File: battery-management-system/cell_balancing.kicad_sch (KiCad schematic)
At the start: 28 parts, among them Q14 DMN3404L, Q15 DMN3404L, Q16 DMN3404L, Q17 DMN3404L, Q18 DMN3404L, Q19 DMN3404L, Q20 DMN3404L, Q21 DMN3404L, Q22 DMN3404L, Q23 DMN3404L, Q24 DMN3404L, Q25 DMN3404L, Q26 DMN3404L, Q27 DMN3404L, Q28 DMN3404L, Q29 DMN3404L, Q30 DMN3404L, Q31 DMN3404L, U16 MC74VHC139

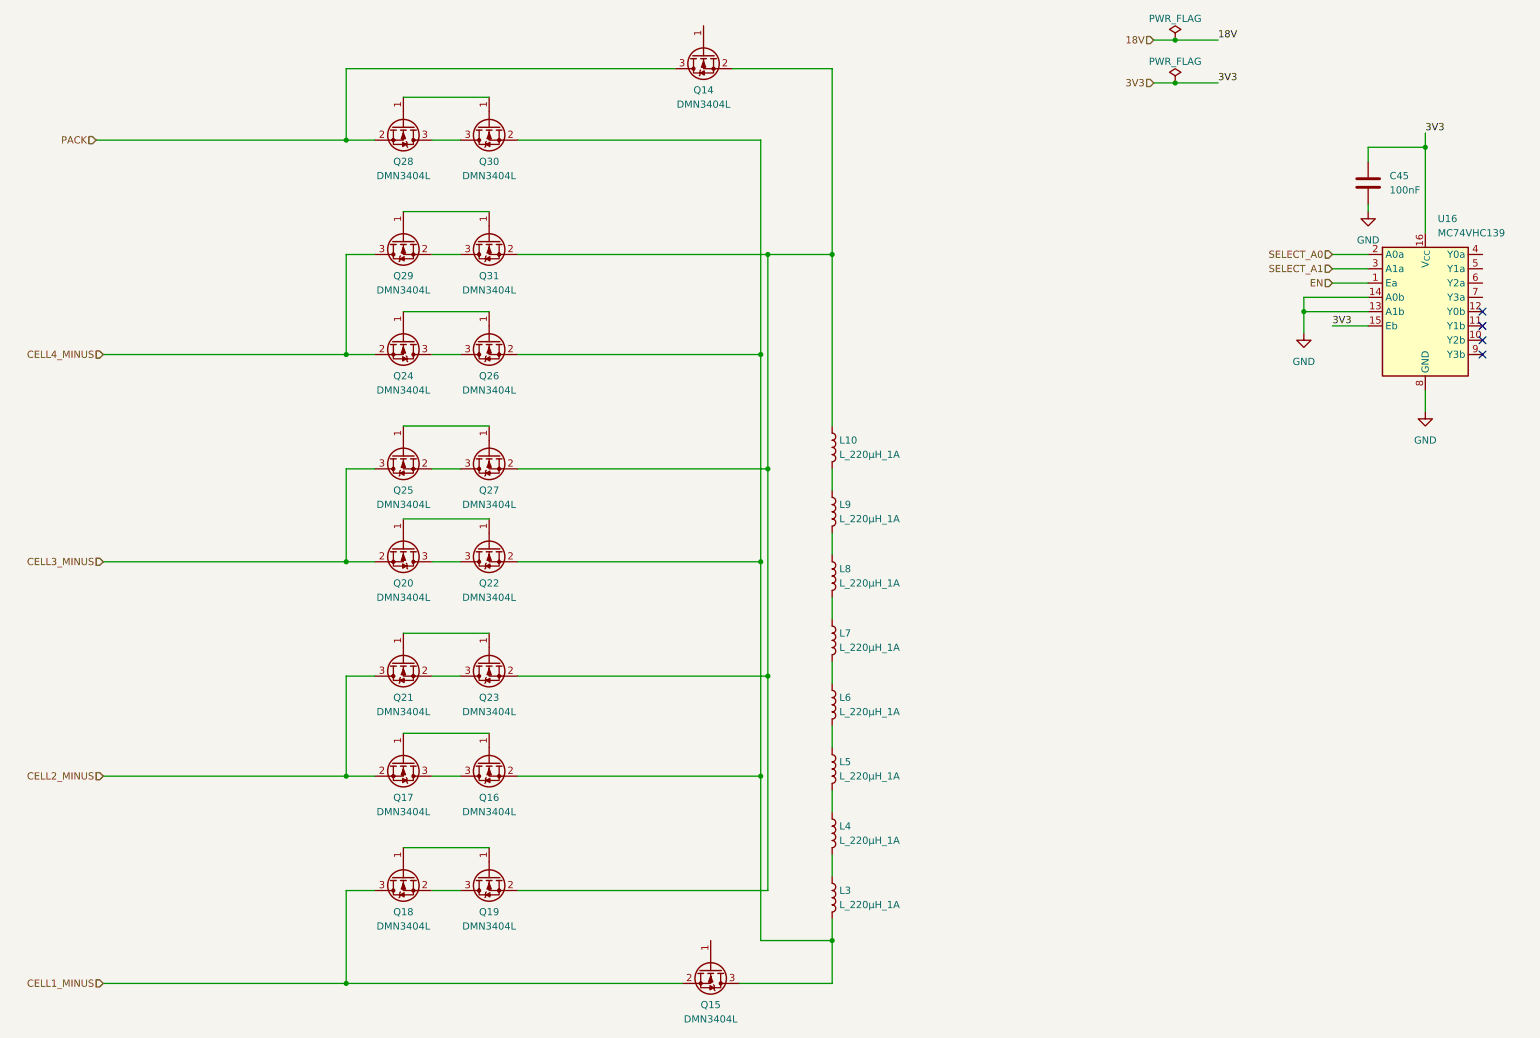
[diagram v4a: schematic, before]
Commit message: finish cell balancing changes
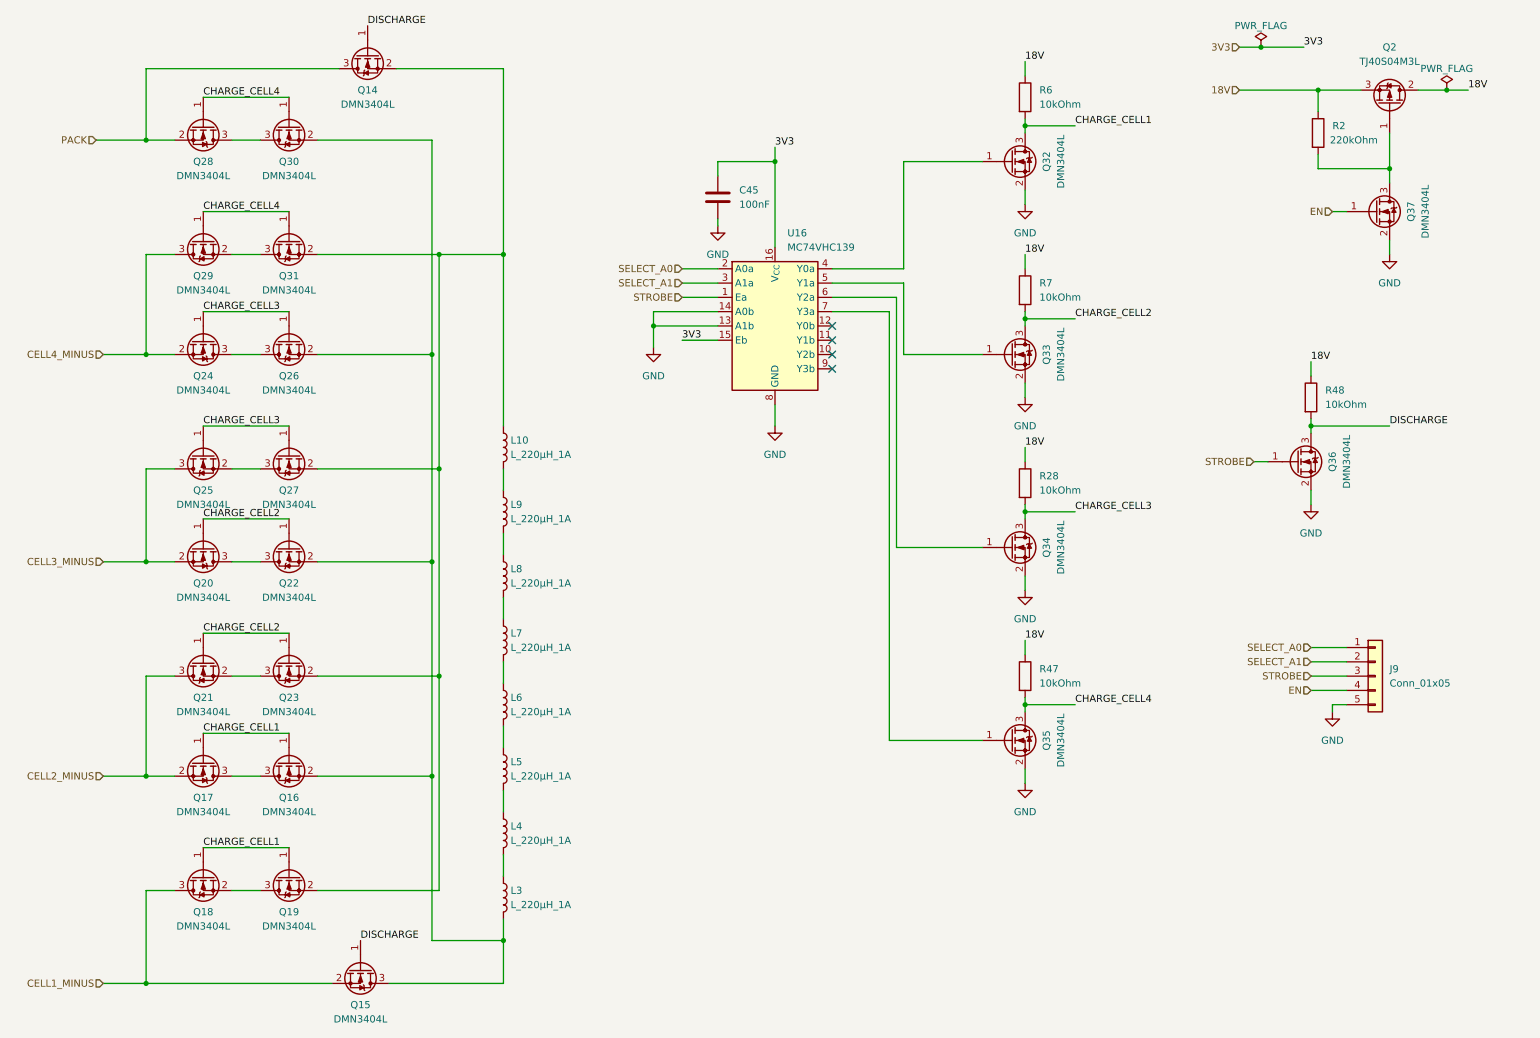
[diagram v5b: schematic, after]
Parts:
- added J9: Conn_01x05, benediktibk:PinHeader_1x05_P2.54mm_Vertical, symbol benediktibk:Conn_01x05
- added Q2: TJ40S04M3L, benediktibk:TO-252-2, symbol benediktibk:TJ40S04M3L
- added Q32, Q33, Q34, Q35, Q36, Q37: DMN3404L, benediktibk:SOT-23, symbol benediktibk:DMN3404L
- added R2: 220kOhm, benediktibk:R_0603_1608Metric_Pad0.98x0.95mm_HandSolder, symbol benediktibk:R_220kOhm_SMD_0603_100mW_1%
- added R28, R47, R48, R6, R7: 10kOhm, benediktibk:R_0603_1608Metric_Pad0.98x0.95mm_HandSolder, symbol benediktibk:R_10kOhm_SMD_0603_100mW_1%
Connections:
- net 18V: now also Q2.2 (D), Q2.3 (S), R2.1, R28.1, R47.1, R48.1, R6.1, R7.1
- net EN: now also J9.4 (Pin_4), Q37.1 (G); no longer U16.1 (Ea)
- net GND: now also J9.5 (Pin_5), Q32.2 (S), Q33.2 (S), Q34.2 (S), Q35.2 (S), Q36.2 (S), Q37.2 (S)
- net SELECT_A0: now also J9.1 (Pin_1)
- net SELECT_A1: now also J9.2 (Pin_2)
- net CHARGE_CELL4: now reaches Q29.1 (G), Q31.1 (G)
- net CHARGE_CELL4: now also Q28.1 (G), Q30.1 (G), Q35.3 (D), R47.2
- net DISCHARGE: now reaches Q14.1 (G)
- net DISCHARGE: now also Q15.1 (G), Q36.3 (D), R48.2
- net CHARGE_CELL2: now reaches Q21.1 (G), Q23.1 (G)
- net CHARGE_CELL2: now also Q20.1 (G), Q22.1 (G), Q33.3 (D), R7.2
- net CHARGE_CELL3: now reaches Q24.1 (G), Q26.1 (G)
- net CHARGE_CELL3: now also Q25.1 (G), Q27.1 (G), Q34.3 (D), R28.2
- net at U16.4 (Y0a): now also Q32.1 (G)
- net at U16.5 (Y1a): now also Q33.1 (G)
- net at U16.6 (Y2a): now also Q34.1 (G)
- net at U16.7 (Y3a): now also Q35.1 (G)
- net CHARGE_CELL1: now reaches Q18.1 (G), Q19.1 (G)
- net CHARGE_CELL1: now also Q16.1 (G), Q17.1 (G), Q32.3 (D), R6.2
- new net: Q2.1 (G), Q37.3 (D), R2.2
- new net STROBE: J9.3 (Pin_3), Q36.1 (G), U16.1 (Ea)
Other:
- moved on the sheet: C45, L10, L3, L4, L5, L6, L7, L8, L9, Q14, Q15, Q16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

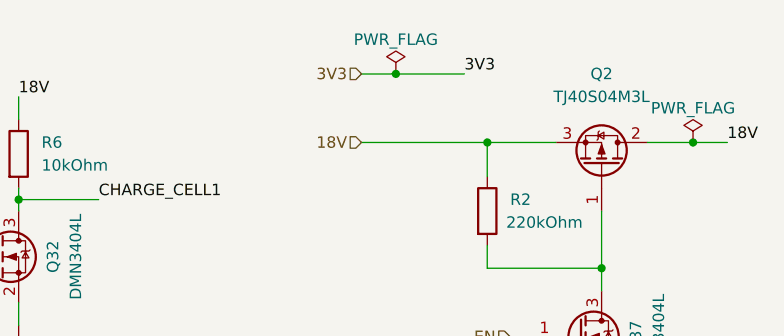
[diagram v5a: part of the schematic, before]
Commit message: fix electrical rule check errors
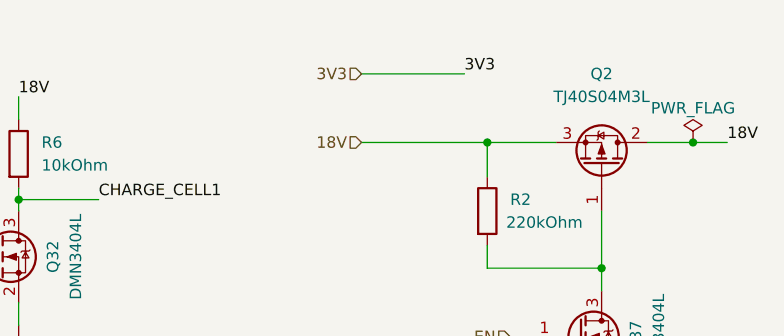
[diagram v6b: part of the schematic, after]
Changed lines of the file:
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@@
   (junction (at 247.65 26.67) (diameter 0) (color 0 0 0 0)
-  )
-  (junction (at 237.49 19.05) (diameter 0) (color 0 0 0 0)
   )
   (junction (at 260.35 40.64) (diameter 0) (color 0 0 0 0)
@@
     (stroke (width 0) (type default))
   )
-  (wire (pts (xy 237.49 19.05) (xy 245.11 19.05))
-    (stroke (width 0) (type default))
-  )
   (wire (pts (xy 195.58 135.89) (xy 204.47 135.89))
     (stroke (width 0) (type default))
@@
     (stroke (width 0) (type default))
   )
-  (wire (pts (xy 233.68 19.05) (xy 237.49 19.05))
+  (wire (pts (xy 233.68 19.05) (xy 245.11 19.05))
     (stroke (width 0) (type default))
   )
@@
         )
       )
-    )
-  )
-  (symbol (lib_id "power:PWR_FLAG") (at 237.49 19.05 0) (unit 1)
-    (in_bom yes) (on_board yes) (dnp no)
-    (property "Reference" "#FLG01" (at 237.49 17.145 0)
-      (effects (font (size 1.27 1.27)) hide)
-    )
-    (property "Value" "PWR_FLAG" (at 237.49 15.24 0)
-      (effects (font (size 1.27 1.27)))
-    )
-    (property "Footprint" "" (at 237.49 19.05 0)
-      (effects (font (size 1.27 1.27)) hide)
-    )
-    (property "Datasheet" "~" (at 237.49 19.05 0)
-      (effects (font (size 1.27 1.27)) hide)
-    )
-    (pin "1")
-    (instances
-      (project "battery-management-system"
-        (path "/5272f0ff-3069-41a9-bca2-80beede8b4b2/b1377397-46a1-4623-af59-88e4e694ca35"
-          (reference "#FLG01") (unit 1)
-        )
-        (path "/5272f0ff-3069-41a9-bca2-80beede8b4b2/3d1b4e38-a765-486c-a970-a0d54d5b41d9"
-          (reference "#FLG010") (unit 1)
-        )
-      )

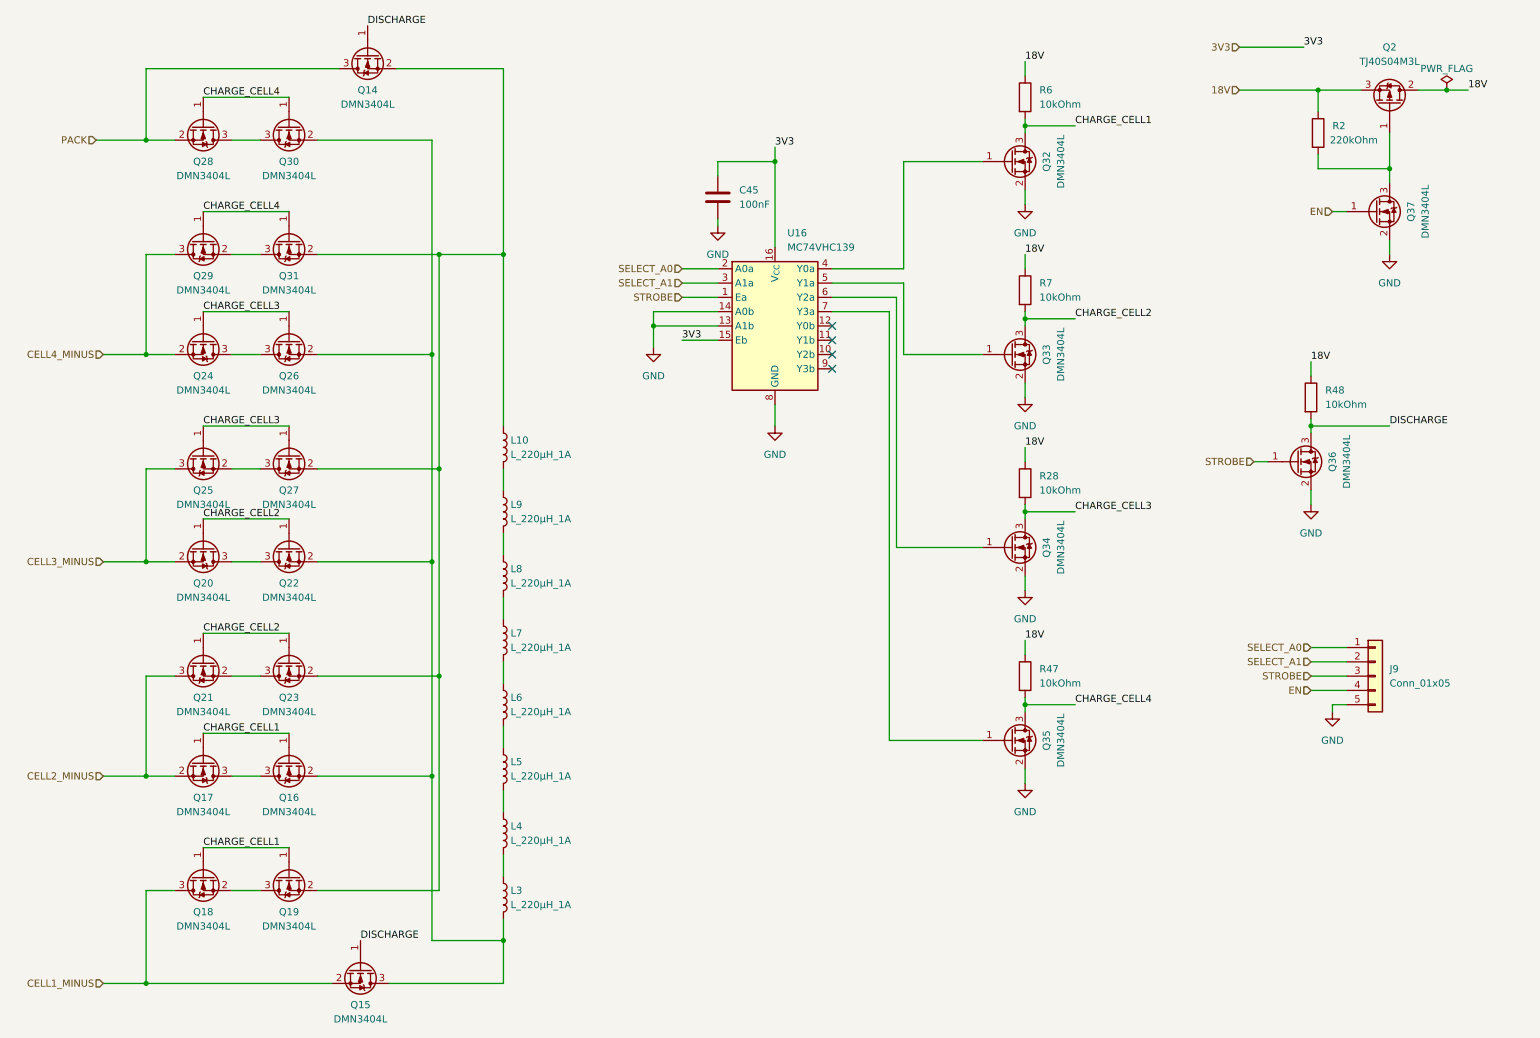
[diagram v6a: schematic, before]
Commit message: add enable input for cell measurement
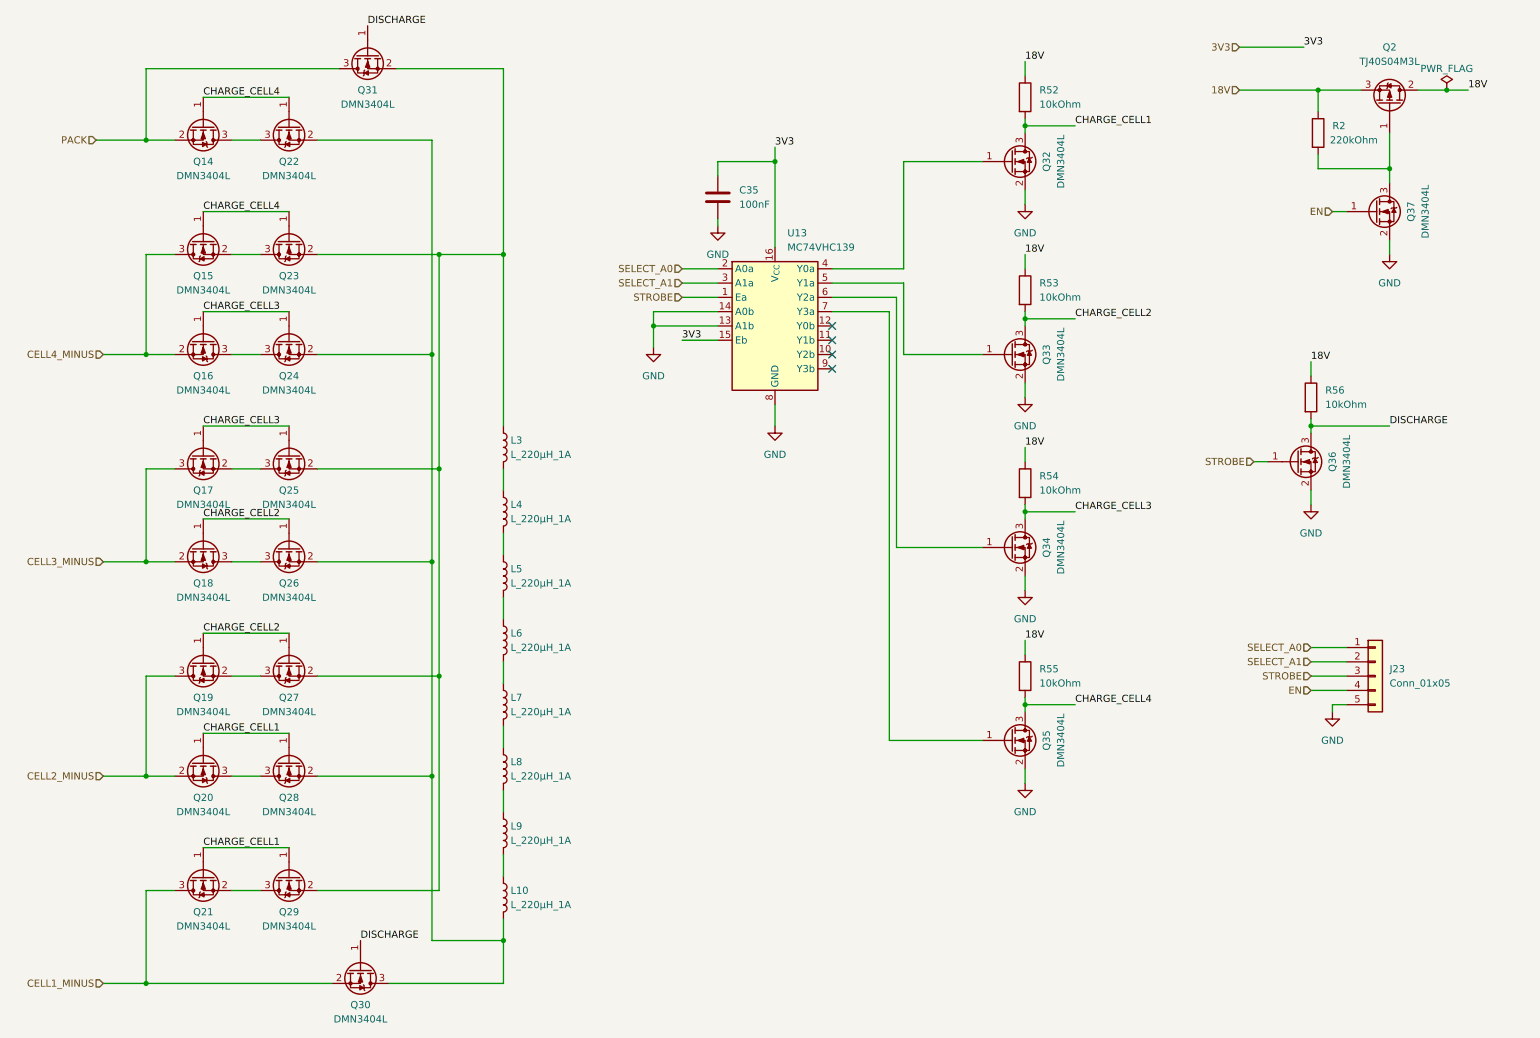
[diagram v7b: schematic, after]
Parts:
- renumbered C45 to C35, J9 to J23, L3 to L10, L10 to L3, L9 to L4, L8 to L5, L7 to L6, L6 to L7, L5 to L8, L4 to L9, Q28 to Q14, Q29 to Q15, Q24 to Q16, Q25 to Q17, Q20 to Q18, Q21 to Q19, Q17 to Q20, Q18 to Q21, Q30 to Q22, Q31 to Q23, Q26 to Q24, Q27 to Q25, Q22 to Q26, Q23 to Q27, Q16 to Q28, Q19 to Q29, Q15 to Q30, Q14 to Q31, R6 to R52, R7 to R53, R28 to R54, R47 to R55, R48 to R56, U16 to U13

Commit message: make layout easier for cell measurement
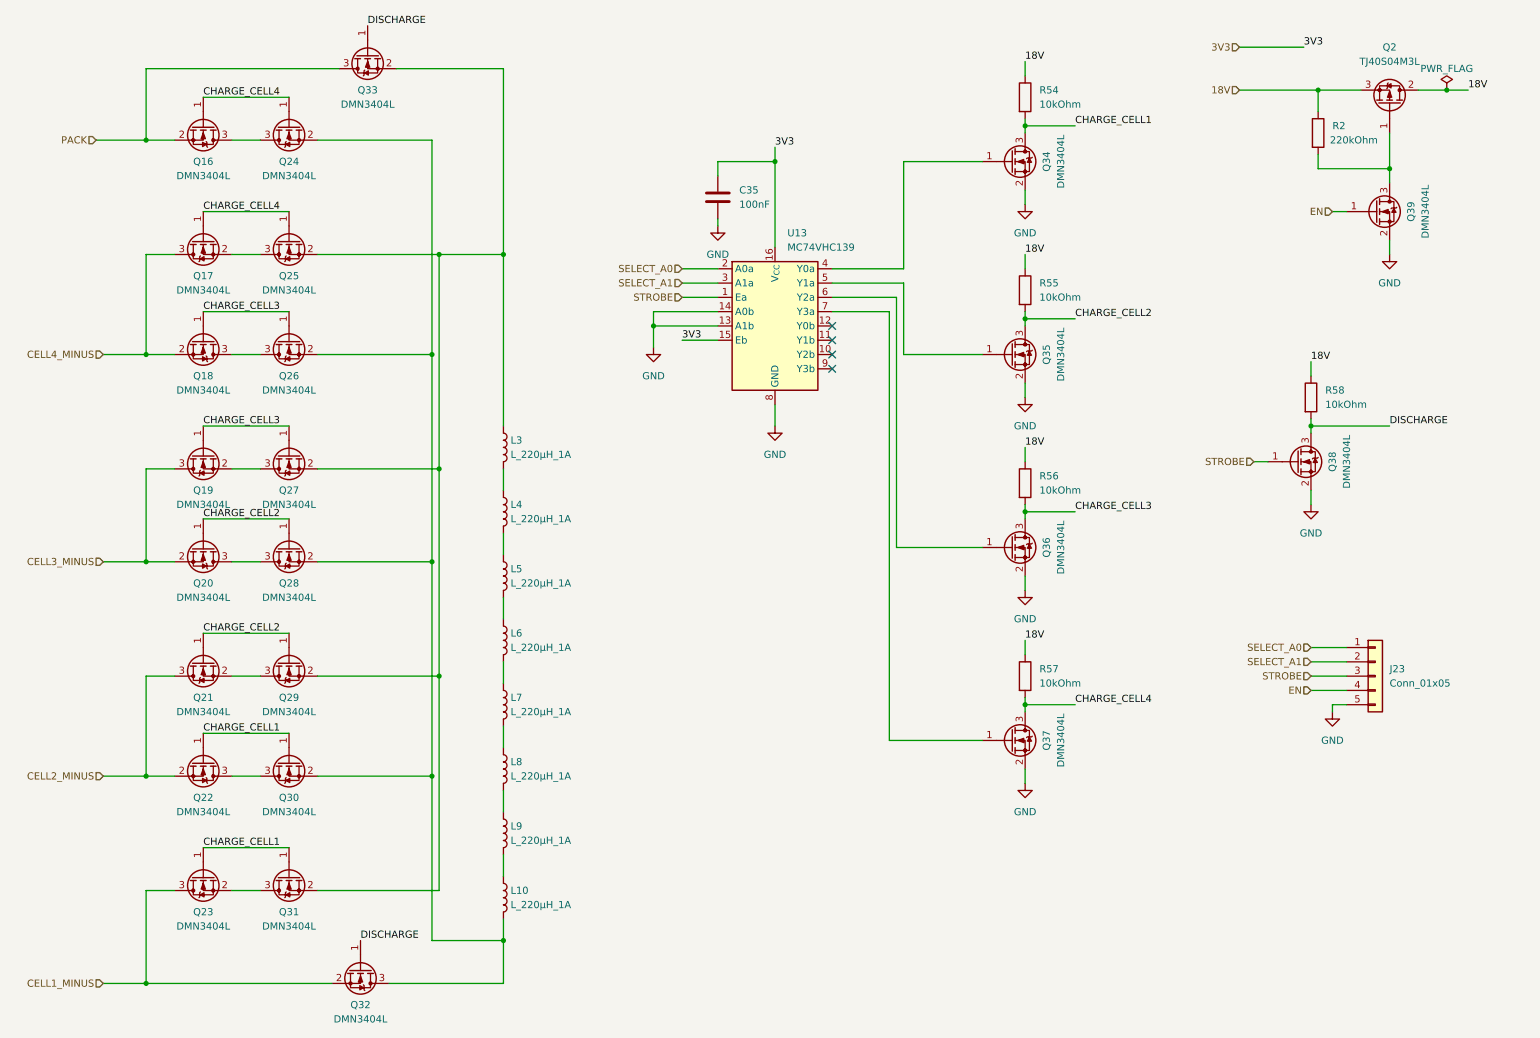
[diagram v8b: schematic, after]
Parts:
- renumbered Q14 to Q16, Q15 to Q17, Q16 to Q18, Q17 to Q19, Q18 to Q20, Q19 to Q21, Q20 to Q22, Q21 to Q23, Q22 to Q24, Q23 to Q25, Q24 to Q26, Q25 to Q27, Q26 to Q28, Q27 to Q29, Q28 to Q30, Q29 to Q31, Q30 to Q32, Q31 to Q33, Q32 to Q34, Q33 to Q35, Q34 to Q36, Q35 to Q37, Q36 to Q38, Q37 to Q39, R52 to R54, R53 to R55, R54 to R56, R55 to R57, R56 to R58
